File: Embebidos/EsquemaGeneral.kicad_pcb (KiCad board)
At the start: 2 copper layers, 79 parts, among them IC1 ESP32-WROVER-B__8MB_, J1 USB_A, J2 Conn_01x02_Male, J3 RJ45, J4 RJ45, J5 Conn_01x04, J6 Conn_02x06_Counter_Clockwise, J7 Conn_01x08, Q1 BC847, Q2 BC847, Q3 BSS138, Q4 DMP3056LSDQ-13, Q5 BSS138, Q6 DMP3056LSDQ-13, SW1 SW_Reset, SW2 SW_Boot, U2 LM358, U3 SPX3819M5-L-3-3, U4 MIC29302WU, U5 MIC5219-3.3YM5

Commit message: organizando
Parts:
- added J8: Conn_01x02, Connector_JST:JST_EH_S2B-EH_1x02_P2.50mm_Horizontal, F.Cu at (89.0, 119.1)
- J6: renamed from J7; footprint Connector_PinHeader_2.54mm:PinHeader_1x08_P2.54mm_Vertical -> Connector_JST:JST_EH_S8B-EH_1x08_P2.50mm_Horizontal
- J7: renamed from J5; footprint Connector_PinHeader_2.54mm:PinHeader_1x04_P2.54mm_Vertical -> Connector_JST:JST_EH_B4B-EH-A_1x04_P2.50mm_Vertical
- moved J3 109.6 mm to (85.1, 80.2), turned to 90 degrees
- moved Q3 103.5 mm to (105.3, 76.3)
- moved Q4 103.5 mm to (107.1, 70.8)
- moved R1a1 103.5 mm to (105.2, 80.0)
- moved R23 103.5 mm to (105.2, 82.9)
- moved R24 103.5 mm to (110.0, 80.0)
- moved R2a1 103.5 mm to (105.2, 85.9)
- moved R3a1 103.5 mm to (110.0, 82.9)
- moved R22 103.5 mm to (110.1, 75.5)
- moved J4 88.7 mm to (85.1, 59.3), turned to 90 degrees
- moved Q5 87.2 mm to (105.2, 54.6)
- moved Q6 87.2 mm to (106.9, 49.1)
- moved R25 87.2 mm to (105.1, 61.2)
- moved R26 87.2 mm to (105.1, 64.2)
- moved R27 87.2 mm to (109.8, 58.3)
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- renumbered J6 to J5
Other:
- board outline added: 100 x 99.9 mm

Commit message: mas orden
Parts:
- moved R10 49.0 mm to (158.7, 94.9)
- moved R11 48.1 mm to (158.6, 98.9)
- moved R12 40.1 mm to (170.6, 74.6), turned to 90 degrees
- moved R5 34.7 mm to (158.7, 79.5)
- moved R8 33.3 mm to (158.7, 86.9)
- moved R4 33.1 mm to (158.7, 83.3)
- moved R9 32.4 mm to (158.8, 90.7)
- moved R7 30.4 mm to (165.7, 74.4), turned to 90 degrees
- moved Q4 26.9 mm to (96.7, 95.6)
- moved JP1 22.4 mm to (104.5, 71.3)
- moved R3 19.2 mm to (120.8, 58.1)
- moved C2 18.9 mm to (126.3, 55.9)
- moved D1 17.9 mm to (115.9, 58.2)
- moved R2 17.2 mm to (126.1, 67.9)
- moved R6 13.1 mm to (120.9, 62.3)
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
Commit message: orden pcb
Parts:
- moved C8 57.9 mm to (132.4, 80.7)
- moved R16 54.9 mm to (137.4, 80.7)
- moved U2 46.7 mm to (138.0, 87.1), turned to 90 degrees
- moved R17 42.4 mm to (146.0, 80.0), turned to -90 degrees
- moved R20 40.8 mm to (139.5, 130.6)
- moved C9 38.6 mm to (145.4, 88.2), turned to 90 degrees
- moved C11 37.4 mm to (113.1, 100.8)
- moved R15 36.2 mm to (132.9, 94.1)
- moved R18 31.4 mm to (144.4, 107.4)
- moved D3 31.4 mm to (137.7, 93.8)
- moved U4 31.2 mm to (140.0, 120.5)
- moved R21 31.1 mm to (156.4, 123.0), turned to 90 degrees
- moved U3 30.9 mm to (114.5, 105.6)
- moved Q4 28.6 mm to (121.3, 81.0)
- moved RV1 28.3 mm to (147.6, 100.7)
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
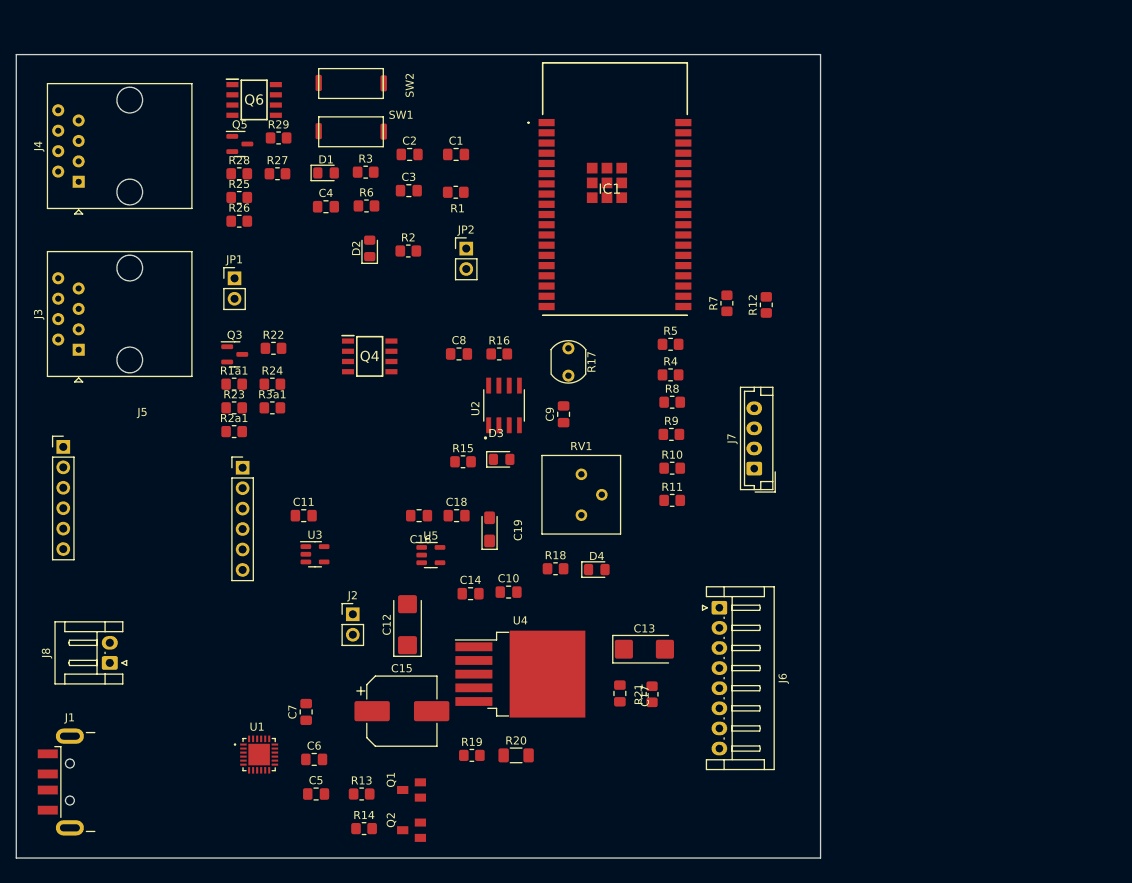
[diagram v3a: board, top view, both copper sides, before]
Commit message: mas orden en la ubicacion de huellas
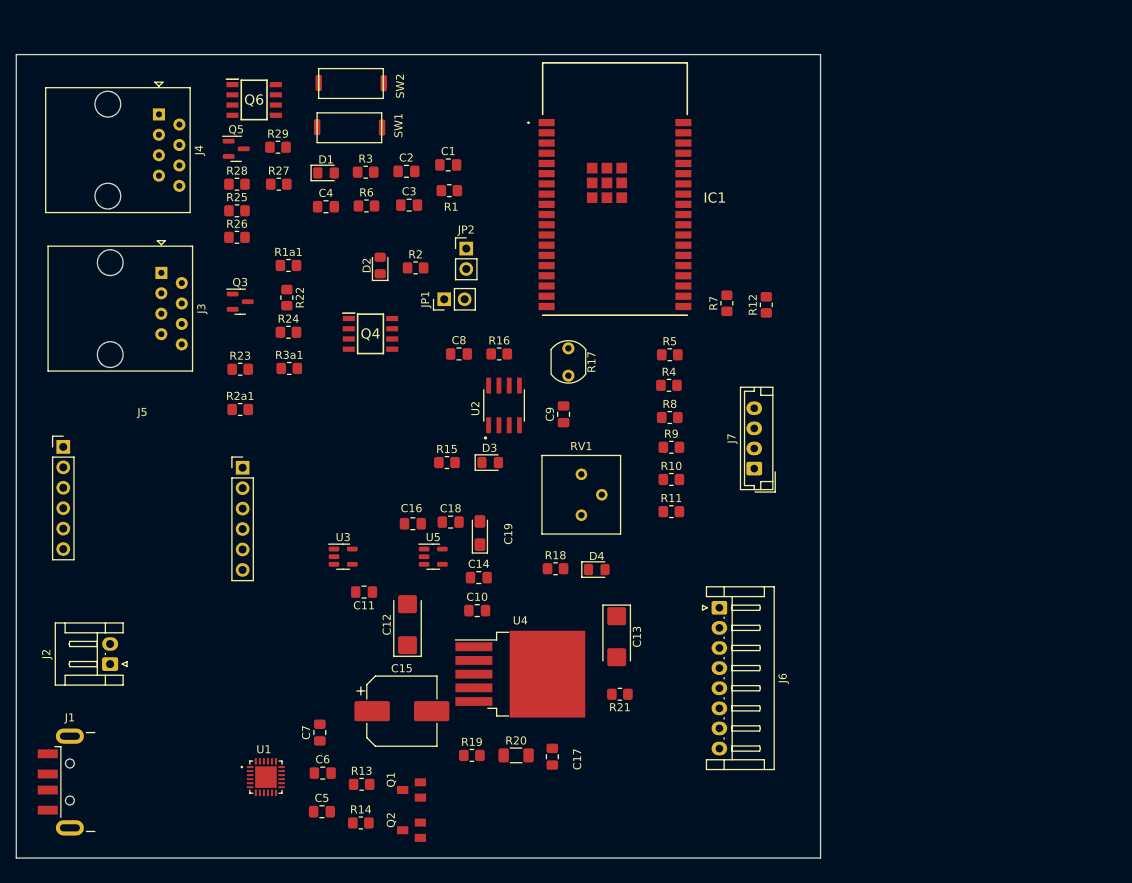
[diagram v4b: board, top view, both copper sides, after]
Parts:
- removed J8: Conn_01x02, Connector_JST:JST_EH_S2B-EH_1x02_P2.50mm_Horizontal
- J2: value Conn_01x02_Male -> Conn_01x02; footprint Connector_PinHeader_2.54mm:PinHeader_1x02_P2.54mm_Vertical -> Connector_JST:JST_EH_S2B-EH_1x02_P2.50mm_Horizontal
- moved J2 30.8 mm to (89.0, 119.2), turned to 90 degrees
- moved JP1 26.2 mm to (130.6, 73.9), turned to 90 degrees
- moved R1a1 16.2 mm to (111.2, 69.7)
- moved J3 14.0 mm to (95.4, 70.6), turned to -90 degrees
- moved J4 13.0 mm to (95.1, 50.9), turned to -90 degrees
- moved C11 12.1 mm to (120.6, 110.3), turned to 180 degrees
- moved C17 11.5 mm to (144.0, 130.8)
- moved R24 6.75 mm to (111.2, 78.0)
- moved Q3 6.59 mm to (105.2, 74.2)
- moved R22 6.52 mm to (111.0, 73.7), turned to -90 degrees
- moved R3a1 5.33 mm to (111.3, 82.5)
- moved R23 4.86 mm to (105.2, 82.6)
- moved C10 4.53 mm to (134.7, 112.6)
- moved R21 4.00 mm to (152.4, 123.0), turned to 180 degrees
- moved C13 3.78 mm to (152.0, 115.8), turned to -90 degrees
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
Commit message: ruteado pero toca corregirlo
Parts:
- moved RV1 30.4 mm to (117.9, 94.6)
- moved C9 13.1 mm to (147.3, 101.2)
- moved R16 11.5 mm to (140.6, 91.7), turned to -90 degrees
- moved R17 10.5 mm to (147.5, 90.4)
- moved C8 9.86 mm to (140.6, 86.2), turned to 90 degrees
- moved R7 7.99 mm to (172.0, 69.4)
- moved IC1 6.60 mm to (158.4, 60.2)
- moved U2 6.18 mm to (133.0, 90.7), turned to 180 degrees
- moved R10 2.41 mm to (158.5, 98.7)
- moved R9 2.41 mm to (158.5, 94.7)
- moved R4 2.41 mm to (158.2, 87.0)
- moved R5 2.41 mm to (158.3, 83.2)
- moved R8 2.41 mm to (158.3, 91.0)
- moved D3 2.41 mm to (136.0, 96.6)
- moved R15 2.41 mm to (130.6, 96.6)
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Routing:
- net GND: track 0.00 -> 593.7 mm, vias 0 -> 6
- net +3.3V: track 0.00 -> 227.1 mm, vias 0 -> 7
- net +5V: track 0.00 -> 192.8 mm, vias 0 -> 2
- net /Acondicionamiento/GPIO0: track 0.00 -> 158.2 mm, vias 0 -> 3
- net /Acondicionamiento/RESET: track 0.00 -> 122.5 mm, vias 0 -> 3
- net /Acondicionamiento/SCL_PAN: track 0.00 -> 118.7 mm
- net /Acondicionamiento/SDA_PAN: track 0.00 -> 102.5 mm
- net /Acondicionamiento/RXSIM: track 0.00 -> 102.1 mm
- net 4.1V: track 0.00 -> 97.8 mm
- net 3.3Vop2: track 0.00 -> 96.2 mm
- net /Acondicionamiento/TXSIM: track 0.00 -> 94.9 mm
- net /Acondicionamiento/RXCP: track 0.00 -> 89.8 mm, vias 0 -> 2
- net /Acondicionamiento/TXCP: track 0.00 -> 88.6 mm, vias 0 -> 2
- net /Acondicionamiento/ctr_trasero: track 0.00 -> 73.6 mm
- net /Acondicionamiento/MOSI_RFID: track 0.00 -> 71.8 mm
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
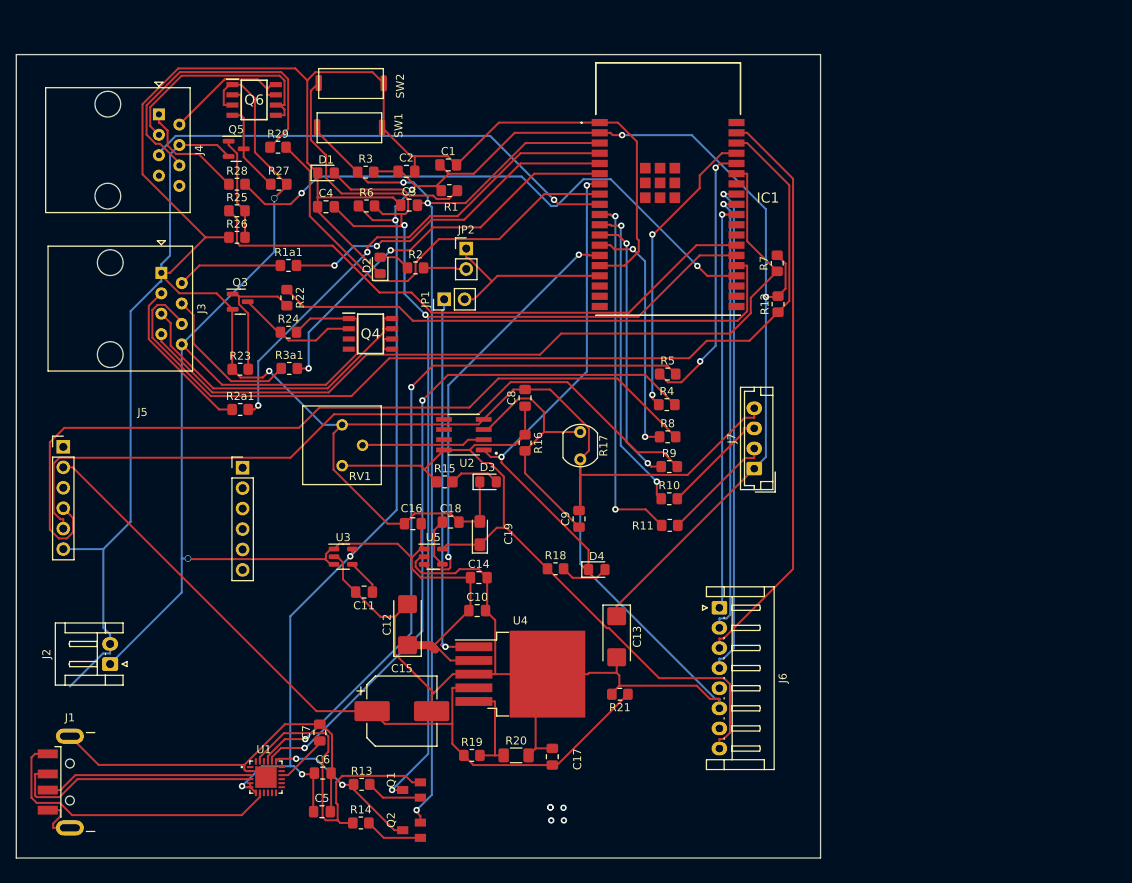
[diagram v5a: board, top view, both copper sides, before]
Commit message: mejora ubicacion de huellas
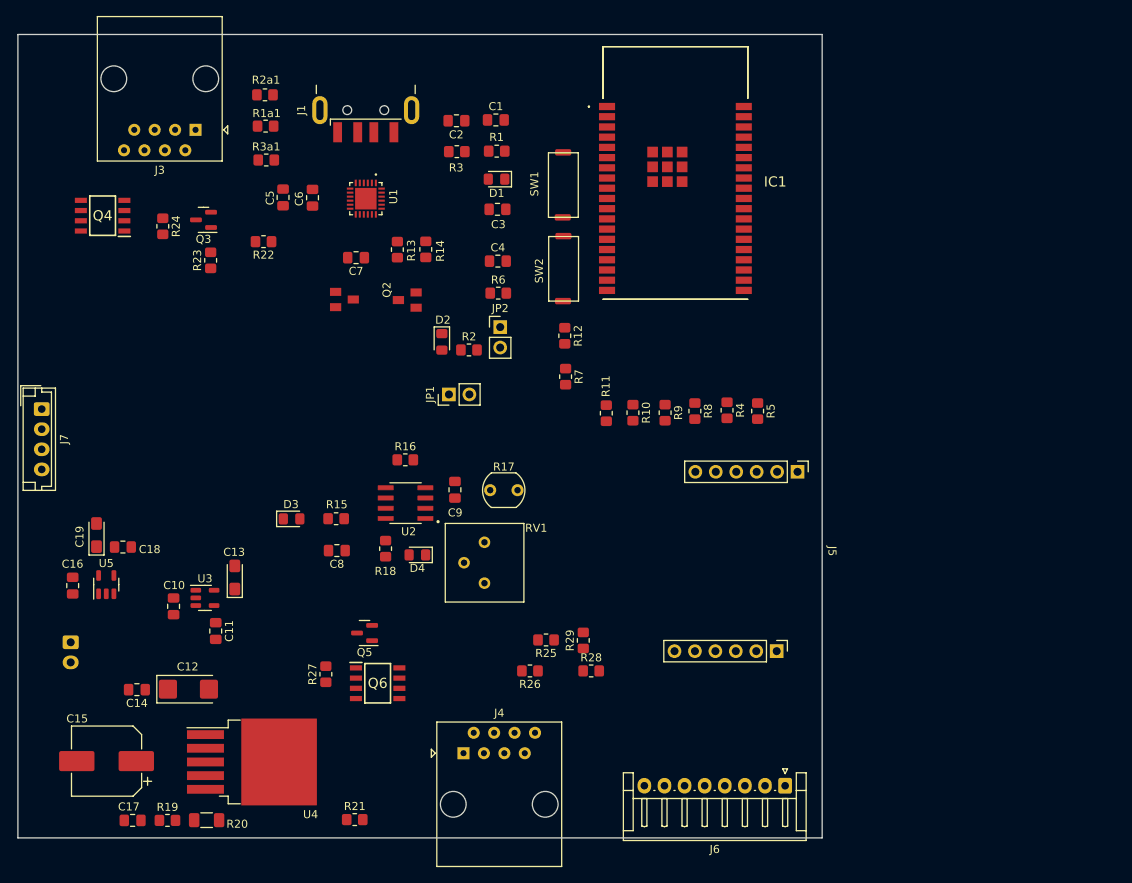
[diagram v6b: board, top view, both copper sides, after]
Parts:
- C13: value 4.7u -> 1U; footprint Capacitor_Tantalum_SMD:CP_EIA-6032-15_Kemet-U_Pad2.25x2.35mm_HandSolder -> Capacitor_Tantalum_SMD:CP_EIA-3216-18_Kemet-A_Pad1.58x1.35mm_HandSolder
- J2: moved to B.Cu
- moved J1 95.2 mm to (120.8, 43.5), turned to 90 degrees
- moved J7 88.9 mm to (80.5, 87.5), turned to -90 degrees
- moved J4 88.0 mm to (133.0, 130.3), turned to 0 degrees
- moved C5 76.5 mm to (110.5, 61.2), turned to -90 degrees
- moved R28 74.8 mm to (148.8, 120.1)
- moved Q6 74.1 mm to (122.3, 121.6)
- moved J5 73.6 mm to (163.1, 101.6), turned to -90 degrees
- moved U1 73.0 mm to (120.8, 61.4), turned to -90 degrees
- moved R29 72.1 mm to (147.8, 116.3), turned to 90 degrees
- moved R14 71.8 mm to (128.3, 67.7), turned to -90 degrees
- moved C6 71.5 mm to (114.2, 61.3), turned to -90 degrees
- moved R13 66.6 mm to (124.7, 67.7), turned to -90 degrees
- moved Q2 65.9 mm to (126.0, 74.0)
- moved R25 65.7 mm to (143.2, 116.2), turned to 180 degrees
- moved R26 65.1 mm to (141.2, 120.1), turned to 180 degrees
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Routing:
- net GND: track 593.7 -> 0.00 mm, vias 6 -> 0
- net +3.3V: track 227.1 -> 0.00 mm, vias 7 -> 0
- net +5V: track 192.8 -> 0.00 mm, vias 2 -> 0
- net /Acondicionamiento/GPIO0: track 158.2 -> 0.00 mm, vias 3 -> 0
- net /Acondicionamiento/RESET: track 122.5 -> 0.00 mm, vias 3 -> 0
- net /Acondicionamiento/SCL_PAN: track 118.7 -> 0.00 mm
- net /Acondicionamiento/SDA_PAN: track 102.5 -> 0.00 mm
- net /Acondicionamiento/RXSIM: track 102.1 -> 0.00 mm
- net 4.1V: track 97.8 -> 0.00 mm
- net 3.3Vop2: track 96.2 -> 0.00 mm
- net /Acondicionamiento/TXSIM: track 94.9 -> 0.00 mm
- net /Acondicionamiento/RXCP: track 89.8 -> 0.00 mm, vias 2 -> 0
- net /Acondicionamiento/TXCP: track 88.6 -> 0.00 mm, vias 2 -> 0
- net /Acondicionamiento/ctr_trasero: track 73.6 -> 0.00 mm
- net /Acondicionamiento/MOSI_RFID: track 71.8 -> 0.00 mm
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
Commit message: pistas gordas :(
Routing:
- net +3.3V: track 0.00 -> 185.0 mm, vias 0 -> 7
- net +5V: track 0.00 -> 181.4 mm
- net /Acondicionamiento/SCL_PAN: track 0.00 -> 140.9 mm, vias 0 -> 1
- net 3.3Vop2: track 0.00 -> 129.0 mm
- net /Acondicionamiento/SDA_PAN: track 0.00 -> 116.6 mm, vias 0 -> 2
- net 4.1V: track 0.00 -> 111.3 mm
- net CtrlOnOff: track 0.00 -> 98.1 mm
- net /Acondicionamiento/MOSI_RFID: track 0.00 -> 90.7 mm
- net /Acondicionamiento/RESET: track 0.00 -> 83.9 mm, vias 0 -> 2
- net /Acondicionamiento/VO_Inf: track 0.00 -> 79.4 mm, vias 0 -> 1
- net /Acondicionamiento/SCK_RFID: track 0.00 -> 78.9 mm, vias 0 -> 1
- net /Acondicionamiento/MISO_RFID: track 0.00 -> 78.3 mm, vias 0 -> 1
- net /Acondicionamiento/CS_RFID: track 0.00 -> 77.3 mm, vias 0 -> 1
- net /Acondicionamiento/RXGPS: track 0.00 -> 75.0 mm, vias 0 -> 2
- net /Acondicionamiento/RXCP: track 0.00 -> 74.8 mm, vias 0 -> 2
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
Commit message: no se uwu
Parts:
- C19: footprint Capacitor_Tantalum_SMD:CP_EIA-3216-12_Kemet-S_Pad1.58x1.35mm_HandSolder -> Capacitor_Tantalum_SMD:CP_EIA-3216-18_Kemet-A_Pad1.58x1.35mm_HandSolder
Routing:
- net +3.3V: track 185.0 -> 1457.2 mm, vias 7 -> 27
- net 4.1V: track 111.3 -> 322.6 mm, vias 0 -> 8
- net +5V: track 181.4 -> 0.00 mm
- net /Acondicionamiento/SCL_PAN: track 140.9 -> 0.00 mm, vias 1 -> 0
- net /Acondicionamiento/SDA_PAN: track 116.6 -> 0.00 mm, vias 2 -> 0
- net CtrlOnOff: track 98.1 -> 0.00 mm
- net Net-(IC1-Pad35): track 35.7 -> 126.3 mm
- net /Acondicionamiento/MOSI_RFID: track 90.7 -> 0.00 mm
- net /Acondicionamiento/RESET: track 83.9 -> 0.00 mm, vias 2 -> 0
- net /Acondicionamiento/VO_Inf: track 79.4 -> 0.00 mm, vias 1 -> 0
- net /Acondicionamiento/RXCP: track 74.8 -> 0.00 mm, vias 2 -> 0
- net /Acondicionamiento/GPIO0: track 74.3 -> 0.00 mm, vias 3 -> 0
- net /Acondicionamiento/Din_izq: track 61.9 -> 0.00 mm, vias 2 -> 0
- net /Acondicionamiento/LDR_IN: track 60.4 -> 0.00 mm, vias 2 -> 0
- net /Acondicionamiento/TXCP: track 59.3 -> 0.00 mm, vias 2 -> 0
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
